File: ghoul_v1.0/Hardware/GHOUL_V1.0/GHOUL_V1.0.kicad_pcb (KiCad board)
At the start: 4 copper layers, 104.1 x 88.9 mm, 44 parts, among them J1 XT30, J2 Conn_01x02, J3 Conn_01x02, M2 Motor_Servo, U1 LM1084-ADJ, U2 DS18S20, U3 Xbee, U4 TPS62133, U5 MS5607-02BA, U6 MAX-M10S, U7 Teensy4.1

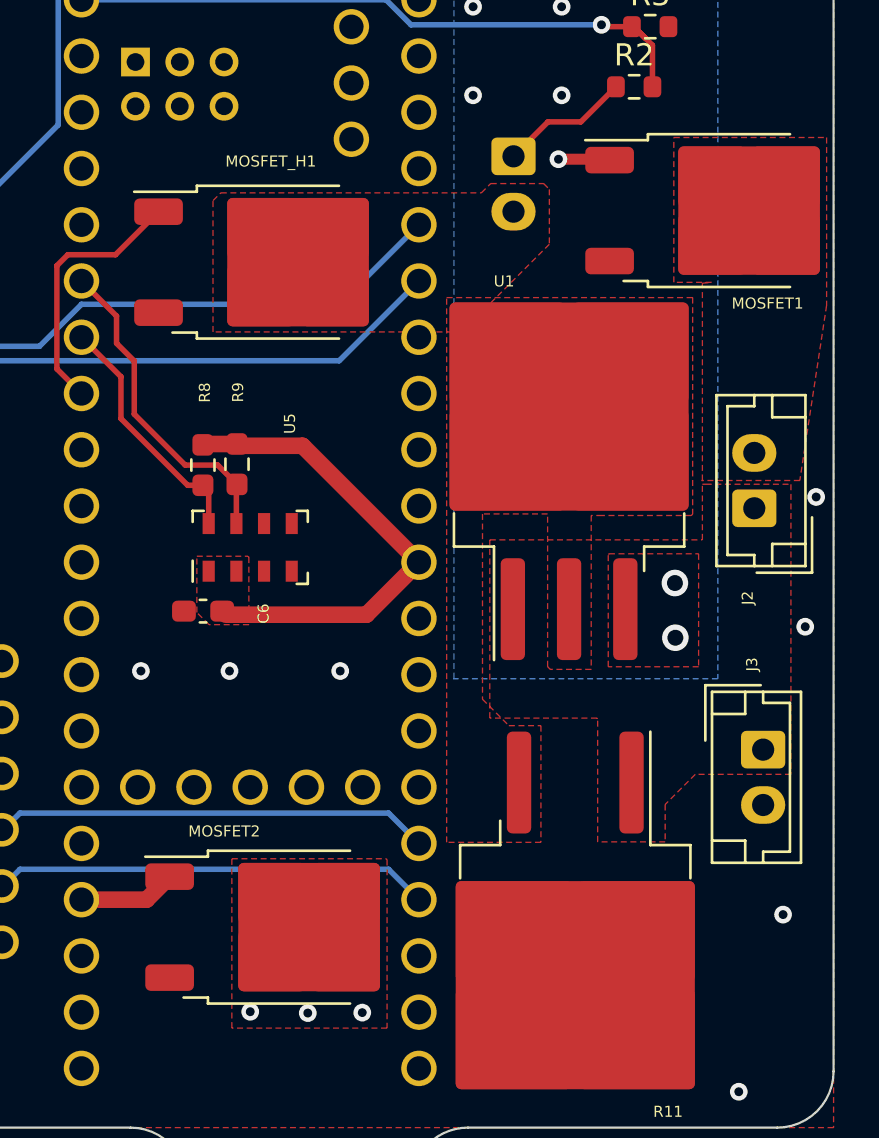
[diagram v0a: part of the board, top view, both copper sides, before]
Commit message: correct BOM for ordering parts
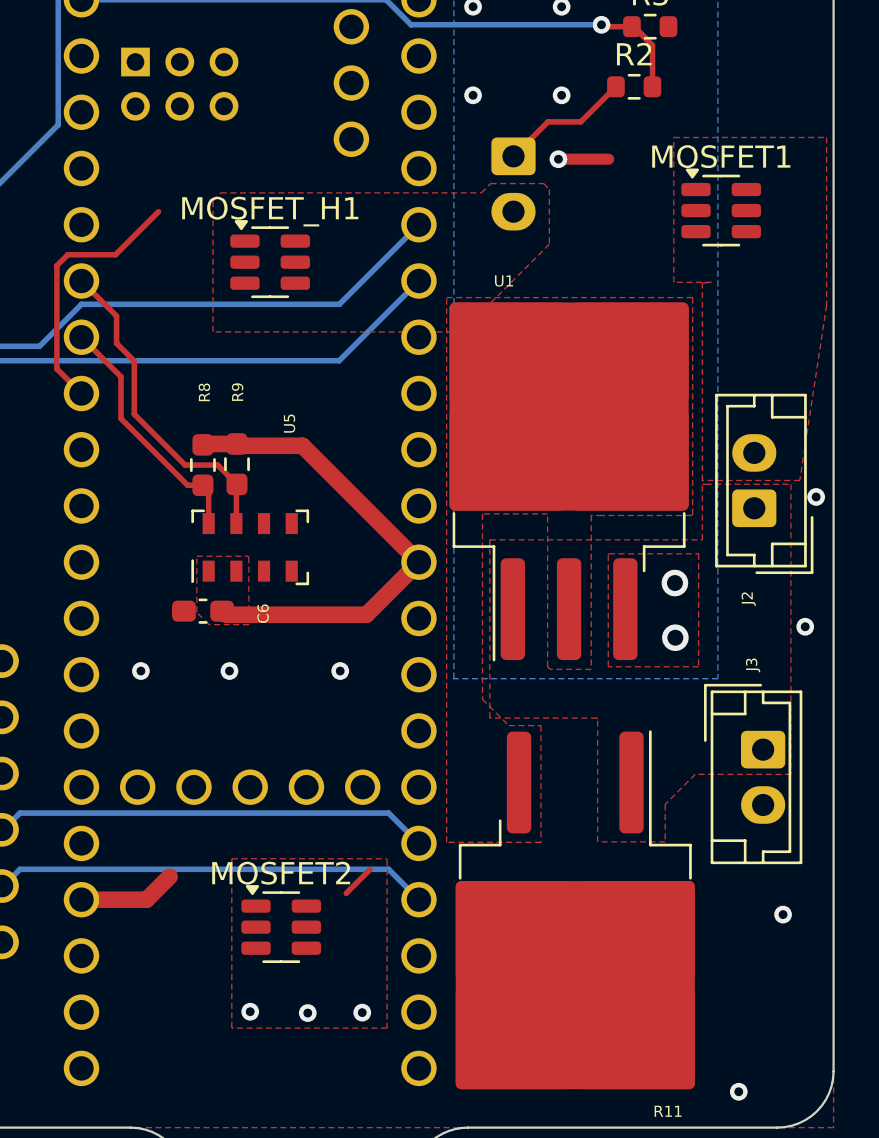
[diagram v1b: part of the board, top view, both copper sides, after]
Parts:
- MOSFET1, MOSFET2, MOSFET_H1: value IRF540N -> FDC637BNZ; footprint Package_TO_SOT_SMD:TO-252-2 -> Package_TO_SOT_SMD:SOT-23-6
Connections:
- U7 pad 45: /feedback -> unconnected-(U7-23_A9_CRX1_MCLK1-Pad45)
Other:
- board text added: "Version 3.0 HAB Helium Venting Board Updated Nov 2025 Produced by: Michael Kalin, Jeremy Kuznetsov, Akemi Takeuchi, Jack Bishop, Logan Thompson Maryland Space Grant Consortium Balloon Payload Program Space Systems Lab Univ. of Maryland, College Park (2025)"
- board text removed: "Version 3.0 HAB Helium Venting Board Produced by: Michael Kalin, Kruti Bhingradiya, Jeremy Kuznetsov, Daniel Grammer, Akemi Takeuchi, and Jack Bishop Maryland Space Grant Consortium Balloon Payload Program Space Systems Lab Univ. of Maryland, College Park (2023)"

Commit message: final akemi changes
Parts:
- removed MOSFET1, MOSFET2, MOSFET_H1: FDC637BNZ, Package_TO_SOT_SMD:SOT-23-6
- added Q1: FDC637BNZ, Package_TO_SOT_SMD:TSOT-23-6, F.Cu at (180.8, 95.3)
- added Q2: FDC637BNZ, Package_TO_SOT_SMD:TSOT-23-6, F.Cu at (181.4, 125.3)
- added Q3: FDC637BNZ, Package_TO_SOT_SMD:TSOT-23-6, F.Cu at (201.6, 93.3)
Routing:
- net /nic1: track 53.2 -> 56.1 mm
- net /nic2: track 4.41 -> 6.18 mm
- net Net-(Q1-G): track 11.8 -> 13.5 mm
- net Net-(J3-Pin_2): track 1.52 -> 0.00 mm

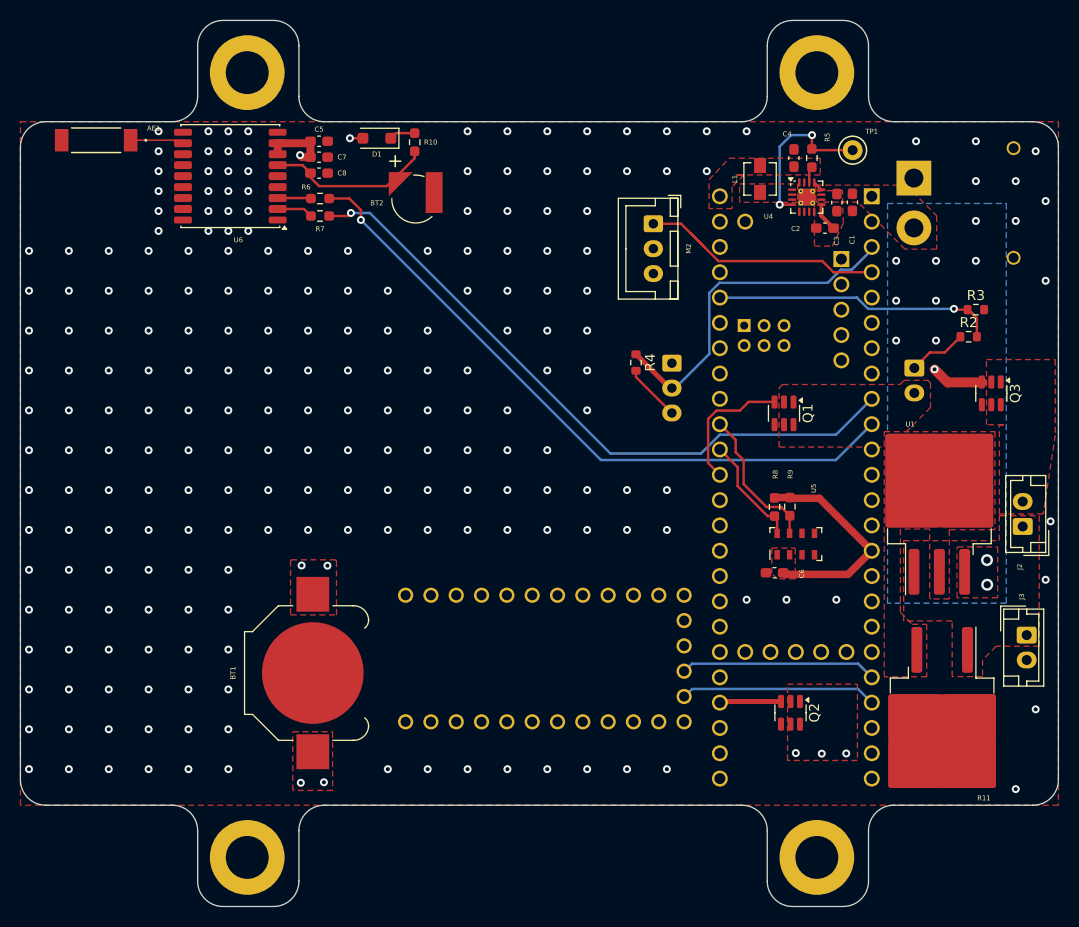
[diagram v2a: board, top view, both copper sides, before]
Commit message: fixed some minor DRC errors, shortened length to reduce manufacture cost
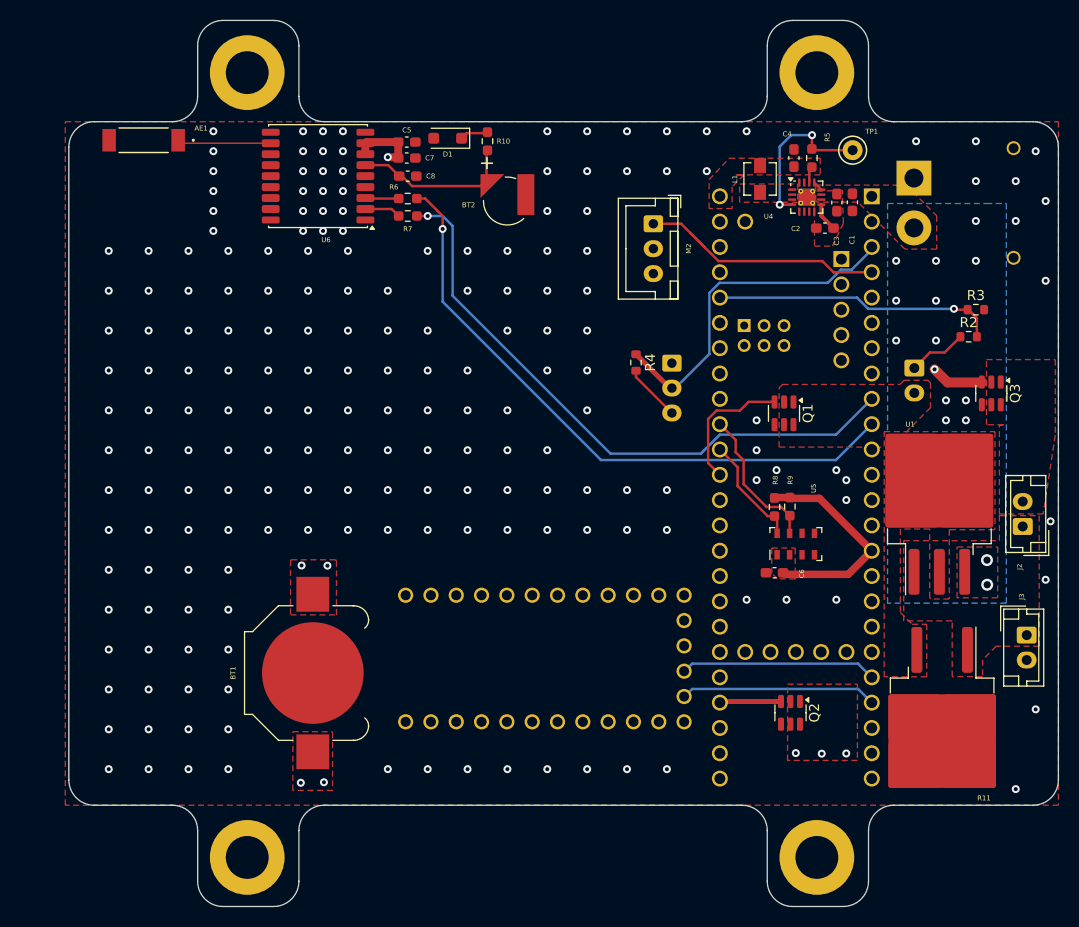
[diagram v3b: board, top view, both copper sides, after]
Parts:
- moved BT2 9.20 mm to (153.0, 74.0)
- moved C8 8.91 mm to (143.0, 71.5)
- moved C5 8.80 mm to (142.9, 68.1)
- moved C7 8.80 mm to (142.9, 69.7)
- moved R6 8.80 mm to (143.0, 73.8)
- moved R7 8.80 mm to (143.0, 75.5)
- moved U6 8.80 mm to (134.0, 71.5)
- moved R10 7.30 mm to (151.0, 68.0)
- moved D1 7.10 mm to (147.0, 67.7)
- moved AE1 4.76 mm to (116.5, 67.9)
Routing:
- net /GPS_TX: track 66.8 -> 61.9 mm
- net /GPS_RX: track 67.4 -> 63.0 mm
- net Net-(AE1-A): track 5.37 -> 9.41 mm
- net +3.3V: track 36.1 -> 34.8 mm, vias 2 -> 1
- net GND: vias 228 -> 205
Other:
- board size 104.1 x 88.9 mm -> 99.3 x 88.9 mm
